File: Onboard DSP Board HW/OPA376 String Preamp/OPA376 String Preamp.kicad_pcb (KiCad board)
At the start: 2 copper layers, 28.4 x 89.9 mm, 48 parts, among them J1 Input, J10 Input, J14 Input, J5 Input, U1 TLV9001IDCK, U2 TLV9001IDCK, U3 TLV9001IDCK, U4 TLV9001IDCK

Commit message: WIP
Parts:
- U1, U2, U3, U4: value TLV9001IDCK -> OPA376
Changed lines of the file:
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@@
 			)
 		)
+		(attr exclude_from_bom)
 		(duplicate_pad_numbers_are_jumpers no)
 		(fp_rect
@@
 			)
 		)
+		(attr exclude_from_bom)
 		(duplicate_pad_numbers_are_jumpers no)
 		(fp_rect
@@
 			)
 		)
+		(attr exclude_from_bom)
 		(duplicate_pad_numbers_are_jumpers no)
 		(fp_rect
@@
 			)
 		)
+		(attr exclude_from_bom)
 		(duplicate_pad_numbers_are_jumpers no)
 		(fp_rect
@@
 			)
 		)
+		(attr exclude_from_bom)
 		(duplicate_pad_numbers_are_jumpers no)
 		(fp_rect
@@
 			)
 		)
+		(attr exclude_from_bom)
 		(duplicate_pad_numbers_are_jumpers no)
 		(fp_rect
@@
 			)
 		)
-		(property "Value" "TLV9001IDCK"
+		(property "Value" "OPA376"
 			(at 0 1.8 0)
 			(layer "F.Fab")
@@
 			)
 		)
+		(attr exclude_from_bom)
 		(duplicate_pad_numbers_are_jumpers no)
 		(fp_rect
@@
 			)
 		)
+		(attr exclude_from_bom)
 		(duplicate_pad_numbers_are_jumpers no)
 		(fp_rect
@@
 			)
 		)
+		(attr exclude_from_bom)
 		(duplicate_pad_numbers_are_jumpers no)
 		(fp_rect
@@
 			)
 		)
+		(attr exclude_from_bom)
 		(duplicate_pad_numbers_are_jumpers no)
 		(fp_rect
@@
 			)
 		)
+		(attr exclude_from_bom)
 		(duplicate_pad_numbers_are_jumpers no)
 		(fp_rect
@@
 			)
 		)
+		(attr exclude_from_bom)
 		(duplicate_pad_numbers_are_jumpers no)
 		(fp_rect
@@
 			)
 		)
-		(property "Value" "TLV9001IDCK"
+		(property "Value" "OPA376"
 			(at 0 1.8 0)
 			(layer "F.Fab")
@@
 			)
 		)
+		(attr exclude_from_bom)
 		(duplicate_pad_numbers_are_jumpers no)
 		(fp_rect
@@
 			)
 		)
+		(attr exclude_from_bom)
 		(duplicate_pad_numbers_are_jumpers no)
 		(fp_rect
@@
 			)
 		)
+		(attr exclude_from_bom)
 		(duplicate_pad_numbers_are_jumpers no)
 		(fp_rect
@@
 			)
 		)
+		(attr exclude_from_bom)
 		(duplicate_pad_numbers_are_jumpers no)
 		(fp_rect
@@
 			)
 		)
-		(property "Value" "TLV9001IDCK"
+		(property "Value" "OPA376"
 			(at 0 1.8 0)
 			(layer "F.Fab")
@@
 			)
 		)
-		(property "Value" "TLV9001IDCK"
+		(property "Value" "OPA376"
 			(at 0 1.8 0)
 			(layer "F.Fab")
@@
 			)
 		)
-		(attr through_hole)
+		(attr through_hole exclude_from_bom)
 		(duplicate_pad_numbers_are_jumpers no)
 		(fp_line

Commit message: WIP
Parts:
- C1, C11, C13, C15: footprint Capacitor_SMD:C_0402_1005Metric -> Capacitor_SMD:C_0603_1608Metric
- C2: value C -> 10uF; footprint Capacitor_SMD:C_0402_1005Metric -> Capacitor_SMD:C_0603_1608Metric
- R1: value R -> 100K
- R2: value R -> 43K
- moved C2 43.2 mm to (100.2, 100.0)
- moved R1 41.0 mm to (101.6, 100.0), turned to 90 degrees
- moved R2 40.8 mm to (102.7, 100.0), turned to -90 degrees
- moved C15 1.08 mm to (96.5, 126.7), turned to 0 degrees
- moved C13 1.07 mm to (96.5, 109.4), turned to 0 degrees
- moved C1 0.99 mm to (96.6, 75.2), turned to 0 degrees
- moved C11 0.98 mm to (96.6, 92.0), turned to 0 degrees
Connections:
- C2 pad 1: /SIngle FET preamp/3.3V -> /SIngle FET preamp/MidRail
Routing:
- net GND: track 16.4 -> 9.89 mm, vias 29 -> 27
- net /SIngle FET preamp/MidRail: track 76.8 -> 82.5 mm
- net /SIngle FET preamp/3.3V: track 101.2 -> 97.8 mm, vias 4 -> 5
- net Net-(C15-Pad2): track 1.11 -> 1.70 mm
- net Net-(C13-Pad2): track 1.11 -> 1.68 mm
- net Net-(C11-Pad2): track 1.11 -> 1.62 mm

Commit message: WIP
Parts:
- moved C1 1.34 mm to (96.6, 73.8)
- moved C16 1.34 mm to (97.5, 126.4)
- moved C17 1.34 mm to (101.1, 70.5)
- moved J1 1.34 mm to (93.4, 67.5)
- moved J14 1.34 mm to (93.4, 122.2)
- moved J16 1.34 mm to (106.6, 122.2)
- moved J2 1.34 mm to (106.6, 77.8)
- moved J3 1.34 mm to (93.4, 77.8)
- moved J4 1.34 mm to (106.6, 67.5)
- moved R22 1.34 mm to (97.5, 125.4)
- moved U1 1.34 mm to (100.0, 72.3)
- moved C10 1.34 mm to (97.5, 71.7)
- moved C15 1.34 mm to (96.5, 128.0)
- moved C20 1.34 mm to (101.1, 125.3)
- moved R13 1.34 mm to (97.5, 70.7)
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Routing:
- net /SIngle FET preamp/MidRail: track 82.5 -> 85.6 mm
- net /SIngle FET preamp2/Output: track 58.0 -> 59.8 mm
- net /SIngle FET preamp/Output: track 22.0 -> 20.6 mm
- net /SIngle FET preamp3/Output: track 75.8 -> 77.1 mm
- net /SIngle FET preamp1/Output: track 40.5 -> 41.4 mm
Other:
- board size 28.4 x 89.9 mm -> 28.4 x 92.7 mm

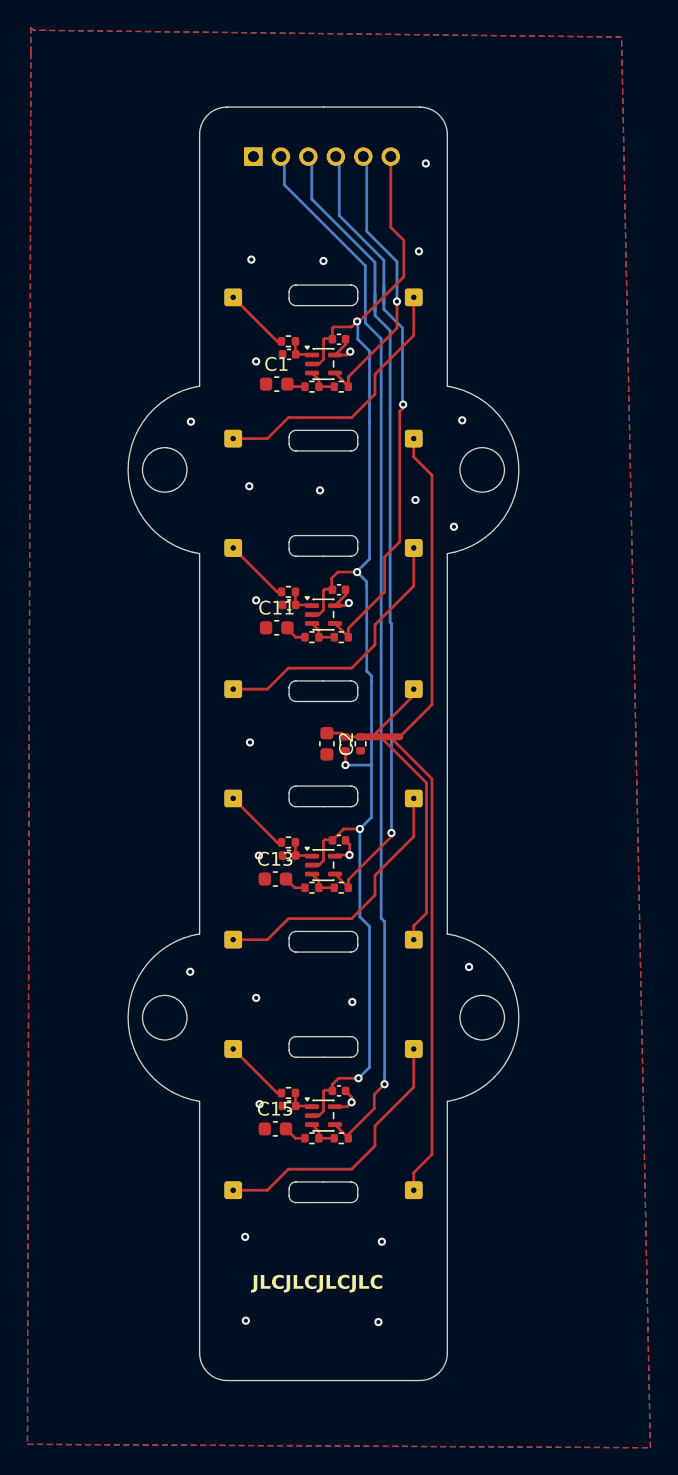
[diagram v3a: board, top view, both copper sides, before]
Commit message: Fix Opamp supplies, simulate, add safety resistor to V+
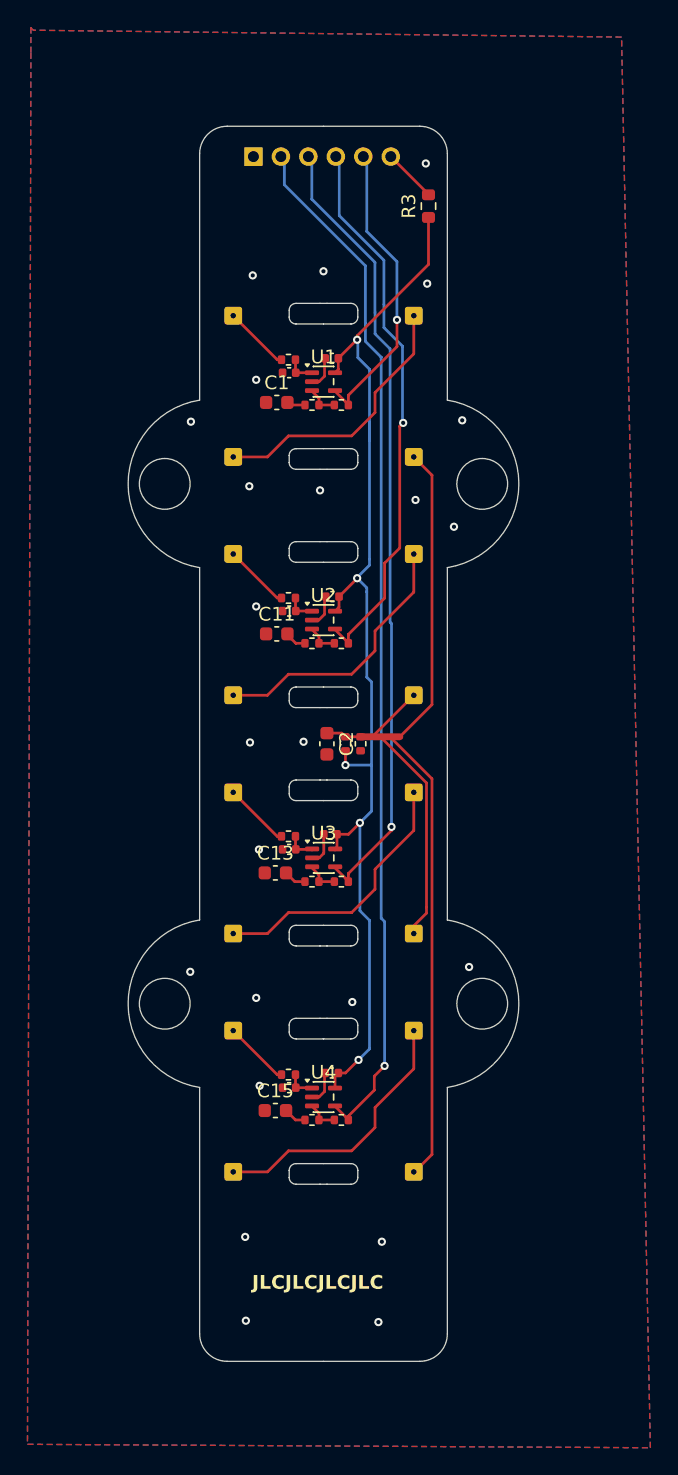
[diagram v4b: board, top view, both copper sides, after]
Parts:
- added R3: 47, Resistor_SMD:R_0603_1608Metric, F.Cu at (107.6, 60.9)
- U1, U2, U3, U4: value OPA376 -> OPA376xxDCK
- moved C17 1.48 mm to (100.6, 71.9), turned to 180 degrees
- moved C20 1.41 mm to (100.6, 124.0), turned to 180 degrees
- moved U4 1.36 mm to (100.0, 125.7)
- moved C1 1.34 mm to (96.6, 75.2)
- moved C16 1.34 mm to (97.5, 125.0)
- moved J1 1.34 mm to (93.4, 68.8)
- moved J14 1.34 mm to (93.4, 120.9)
- moved J16 1.34 mm to (106.6, 120.9)
- moved J2 1.34 mm to (106.6, 79.1)
- moved J3 1.34 mm to (93.4, 79.1)
- moved J4 1.34 mm to (106.6, 68.8)
- moved R22 1.34 mm to (97.5, 124.1)
- moved C10 1.34 mm to (97.5, 73.0)
- moved C15 1.34 mm to (96.5, 126.7)
- moved R13 1.34 mm to (97.5, 72.0)
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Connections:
- net Net-(J1-Pin_1) renamed /Input
- net Net-(J10-Pin_1) renamed /SIngle FET preamp2/Input
- net Net-(J14-Pin_1) renamed /SIngle FET preamp3/Input
- net Net-(J5-Pin_1) renamed /SIngle FET preamp1/Input
- J9 pad 6: /SIngle FET preamp/3.3V -> Net-(J9-Pin_6)
- U1 pad 2: /SIngle FET preamp/3.3V -> GND
- U1 pad 5: GND -> /SIngle FET preamp/3.3V
- U2 pad 2: /SIngle FET preamp/3.3V -> GND
- U2 pad 5: GND -> /SIngle FET preamp/3.3V
- U3 pad 2: /SIngle FET preamp/3.3V -> GND
- U3 pad 5: GND -> /SIngle FET preamp/3.3V
- U4 pad 2: /SIngle FET preamp/3.3V -> GND
- U4 pad 5: GND -> /SIngle FET preamp/3.3V
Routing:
- net /SIngle FET preamp/3.3V: track 97.9 -> 82.5 mm
- net Net-(J9-Pin_6): track 0.00 -> 4.07 mm
- net /SIngle FET preamp/MidRail: track 85.6 -> 82.0 mm
- net /SIngle FET preamp2/Output: track 59.8 -> 58.0 mm
- net /SIngle FET preamp/Output: track 20.6 -> 22.0 mm
- net /SIngle FET preamp3/Output: track 77.1 -> 75.8 mm
- net /SIngle FET preamp1/Output: track 41.4 -> 40.5 mm
- net GND: track 9.89 -> 9.63 mm, vias 27 -> 22
- net (no net): vias 0 -> 2
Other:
- board size 28.4 x 92.7 mm -> 28.4 x 89.9 mm
